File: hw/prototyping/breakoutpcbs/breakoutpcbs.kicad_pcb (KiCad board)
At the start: 2 copper layers, 34.5 x 20.8 mm, 48 parts, among them IC1 LTC2943IDD#TRPBF, J1 Conn_01x05, J2 Conn_01x05, J3 Conn_01x05, J4 Conn_01x05, Q1 BC847, Q2 BC337, Q3 BC337, Q4 SiS415DNT, Q5 BC847, Q6 BC337, Q7 BC847, U1 INA219BxDCN, U2 BD48ExxG, U3 BD48ExxG, U4 L7805, U5 XC6220B331MR, U6 MAX40200AUK

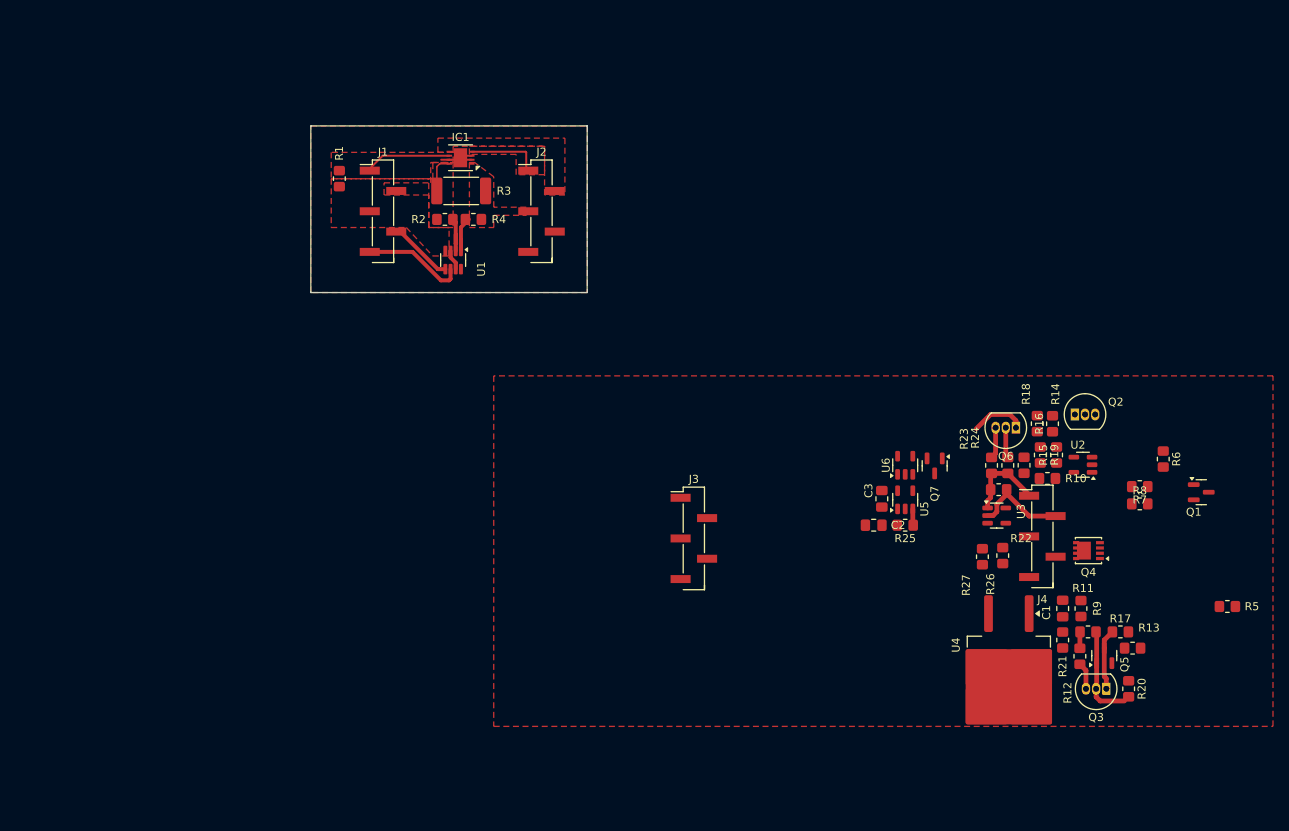
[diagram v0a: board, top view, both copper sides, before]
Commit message: created two other modules to test the switching between charging and runnig mode
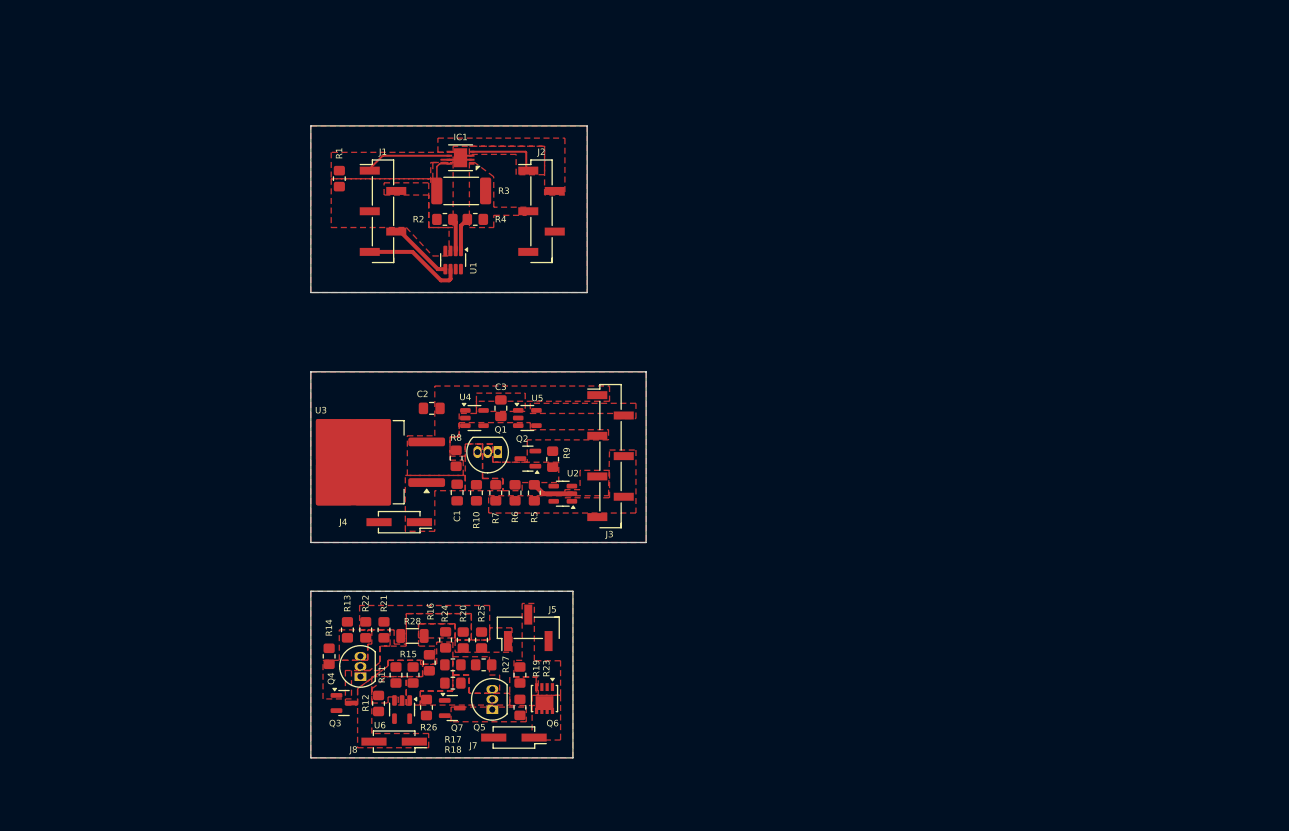
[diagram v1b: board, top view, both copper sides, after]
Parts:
- added J5: Conn_01x03, Connector_PinHeader_2.54mm:PinHeader_1x03_P2.54mm_Vertical_SMD_Pin1Left, F.Cu at (141.7, 118.1)
- added J7: Conn_01x02, Connector_PinHeader_2.54mm:PinHeader_2x01_P2.54mm_Vertical_SMD, F.Cu at (139.9, 131.8)
- added J8: Conn_01x02, Connector_PinHeader_2.54mm:PinHeader_2x01_P2.54mm_Vertical_SMD, F.Cu at (125.0, 132.3)
- added R28: 0R, Resistor_SMD:R_1206_3216Metric, F.Cu at (127.3, 119.1)
- J3: value Conn_01x05 -> Conn_01x07; footprint Connector_PinHeader_2.54mm:PinHeader_1x05_P2.54mm_Vertical_SMD_Pin1Left -> Connector_PinHeader_2.54mm:PinHeader_1x07_P2.54mm_Vertical_SMD_Pin1Left
- J4: value Conn_01x05 -> Conn_01x02; footprint Connector_PinHeader_2.54mm:PinHeader_1x05_P2.54mm_Vertical_SMD_Pin1Left -> Connector_PinHeader_2.54mm:PinHeader_2x01_P2.54mm_Vertical_SMD
- Q1, Q5: value BC847 -> BC337; footprint Package_TO_SOT_SMD:SOT-23 -> Package_TO_SOT_THT:TO-92_Inline
- Q2, Q3: value BC337 -> BC847; footprint Package_TO_SOT_THT:TO-92_Inline -> Package_TO_SOT_SMD:SOT-23
- Q4: value SiS415DNT -> BC337; footprint Package_SO:Vishay_PowerPAK_1212-8_Single -> Package_TO_SOT_THT:TO-92_Inline
- Q6: value BC337 -> SiS415DNT; footprint Package_TO_SOT_THT:TO-92_Inline -> Package_SO:Vishay_PowerPAK_1212-8_Single
- R11: value 4k2 -> 50k
- R12: value 4k2 -> 100k
- R13, R25: value 10k -> 0R
- R15, R23, R8: value 4k2 -> 10k
- R16, R24: value 4k2 -> 0R
- R17, R9: value 10k -> 4k2
- R18, R21, R7: value 0R -> 4k2
- R19: value 0R -> 10k
- R22: value 47k -> 4k2
- R5: value 50k -> 47k
- R6: value 100k -> 4k2
- U3: value BD48ExxG -> L7805; footprint Package_TO_SOT_SMD:SOT-23-5 -> Package_TO_SOT_SMD:TO-263-2
- U4: value L7805 -> XC6220B331MR; footprint Package_TO_SOT_SMD:TO-263-2 -> Package_TO_SOT_SMD:SOT-23-5
- U5: value XC6220B331MR -> MAX40200AUK
- U6: value MAX40200AUK -> BD48ExxG
- moved R13 98.2 mm to (119.1, 118.4), turned to -90 degrees
- moved Q3 95.3 mm to (118.7, 127.5), turned to 0 degrees
- moved Q4 92.4 mm to (120.8, 124.2), turned to 90 degrees
- moved R14 90.1 mm to (116.8, 121.7), turned to -90 degrees
- moved Q1 88.1 mm to (137.9, 96.1), turned to 180 degrees
- moved R12 87.9 mm to (123.0, 127.6), turned to 90 degrees
- moved R5 87.8 mm to (142.5, 101.2), turned to 90 degrees
- moved R11 86.7 mm to (125.2, 124.0), turned to 90 degrees
- moved R8 85.6 mm to (132.7, 96.9), turned to -90 degrees
- moved R15 85.0 mm to (127.3, 124.0)
- moved R21 84.8 mm to (123.7, 118.4)
- moved R17 83.7 mm to (132.3, 125.0)
- moved R16 83.4 mm to (129.4, 122.5), turned to -90 degrees
- moved R20 83.4 mm to (133.6, 119.6), turned to 90 degrees
- moved R6 81.1 mm to (140.1, 101.2), turned to 90 degrees
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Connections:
- C1 pad 1: /power_switch_bb/ONOFF -> /power_switch_bbB/ONOFF
- C1 pad 2: GND -> GND2
- C2 pad 2: GND -> GND2
- C3 pad 1: Net-(U5-VOUT) -> Net-(U4-VOUT)
- C3 pad 2: GND -> GND2
- J3 pad 2: /power_switch_bb/ONOFF -> +3V3_1
- J3 pad 3: /power_switch_bb/VBATT -> /power_switch_bbB/RUNNING
- J3 pad 4: +3V3 -> /power_switch_bbB/EN
- J3 pad 5: GND -> /power_switch_bbB/VBUS
- J4 pad 1: /power_switch_bb/EN -> /power_switch_bbB/ONOFF
- J4 pad 2: /power_switch_bb/VBUS -> GND2
- Q1 pad 1: Net-(Q1-B) -> /power_switch_bbB/RUNNING
- Q1 pad 2: GND -> Net-(Q1-B)
- Q1 pad 3: Net-(Q1-C) -> Net-(Q1-E)
- Q2 pad 1: Net-(Q1-C) -> Net-(Q1-B)
- Q2 pad 2: Net-(Q1-B) -> GND2
- Q2 pad 3: Net-(Q2-E) -> /power_switch_bbB/RUNNING
- Q3 pad 1: Net-(Q3-C) -> Net-(Q3-B)
- Q3 pad 2: Net-(Q3-B) -> GND1
- Q3 pad 3: Net-(Q3-E) -> Net-(Q3-C)
- Q4 pad 1: /power_switch_bb/VBATT -> Net-(Q3-C)
- Q4 pad 2: /power_switch_bb/VBATT -> Net-(Q3-B)
- Q4 pad 3: /power_switch_bb/VBATT -> Net-(Q4-E)
- Q5 pad 1: Net-(Q3-B) -> Net-(Q5-C)
- Q5 pad 2: GND -> Net-(Q5-B)
- Q5 pad 3: Net-(Q3-C) -> Net-(Q5-E)
- Q6 pad 1: /power_switch_bb/RUNNING -> /power_switch_bbA/VBATT
- Q6 pad 2: Net-(Q6-B) -> /power_switch_bbA/VBATT
- Q6 pad 3: Net-(Q6-E) -> /power_switch_bbA/VBATT
- Q7 pad 1: Net-(Q6-B) -> Net-(Q5-B)
- Q7 pad 2: GND -> GND1
- Q7 pad 3: /power_switch_bb/RUNNING -> Net-(Q5-C)
- R10 pad 1: Net-(Q1-C) -> GND2
- R10 pad 2: Net-(U2-VOUT) -> Net-(Q1-E)
- R11 pad 1: Net-(U2-VOUT) -> Net-(U6-VDD)
- R11 pad 2: Net-(Q3-B) -> /power_switch_bbA/ONOFF
- R12 pad 1: Net-(U2-VOUT) -> GND1
- R12 pad 2: Net-(Q3-E) -> Net-(U6-VDD)
- R13 pad 1: /power_switch_bb/VBATT -> GND1
- R13 pad 2: Net-(Q4-G) -> Net-(Q4-E)
- R14 pad 1: /power_switch_bb/EN -> GND1
- R14 pad 2: Net-(Q1-C) -> Net-(Q3-B)
- R15 pad 1: Net-(R15-Pad1) -> Net-(U6-VOUT)
- R15 pad 2: Net-(Q1-B) -> /power_switch_bbA/ONOFF
- R16 pad 1: Net-(R15-Pad1) -> Net-(Q3-C)
- R16 pad 2: Net-(Q2-E) -> Net-(U6-VOUT)
- R17 pad 1: Net-(Q3-C) -> Net-(U6-VOUT)
- R17 pad 2: Net-(Q4-G) -> Net-(Q5-B)
- R18 pad 1: Net-(R15-Pad1) -> Net-(U6-VOUT)
- R18 pad 2: Net-(U2-VOUT) -> Net-(Q5-E)
- R19 pad 1: /power_switch_bb/EN -> /power_switch_bbA/VBATT
- R19 pad 2: Net-(R15-Pad1) -> Net-(Q6-G)
- R20 pad 1: GND -> /power_switch_bbA/EN1
- R20 pad 2: Net-(Q3-B) -> Net-(Q3-C)
- R21 pad 1: GND -> Net-(R21-Pad1)
- R21 pad 2: Net-(Q3-E) -> Net-(Q3-B)
- R22 pad 1: /power_switch_bb/EN -> Net-(R21-Pad1)
- R22 pad 2: /power_switch_bb/VBUS -> Net-(Q4-E)
- R23 pad 1: /power_switch_bb/EN -> Net-(Q5-C)
- R23 pad 2: Net-(Q6-B) -> Net-(Q6-G)
- R24 pad 1: /power_switch_bb/EN -> Net-(R24-Pad1)
- R24 pad 2: Net-(Q6-E) -> Net-(U6-VOUT)
- R25 pad 1: /power_switch_bb/RUNNING -> /power_switch_bbA/EN1
- R25 pad 2: +5V -> Net-(R21-Pad1)
- R26 pad 1: GND -> GND1
- R26 pad 2: Net-(Q6-B) -> Net-(Q5-B)
- R27 pad 1: GND -> GND1
- R27 pad 2: Net-(Q6-E) -> Net-(Q5-E)
- R5 pad 1: Net-(U2-VDD) -> /power_switch_bbB/EN
- R5 pad 2: /power_switch_bb/ONOFF -> /power_switch_bbB/VBUS
- R6 pad 1: GND -> /power_switch_bbB/EN
- R6 pad 2: Net-(U2-VDD) -> Net-(Q1-B)
- R7 pad 1: GND -> /power_switch_bbB/EN
- R7 pad 2: Net-(Q2-E) -> Net-(Q1-E)
- R8 pad 1: GND -> /power_switch_bbB/RUNNING
- R8 pad 2: Net-(Q1-B) -> +5V
- R9 pad 1: Net-(U2-VOUT) -> GND2
- R9 pad 2: /power_switch_bb/ONOFF -> Net-(Q1-B)
- U2 pad 1: Net-(U2-VOUT) -> /power_switch_bbB/EN
- U2 pad 2: Net-(U2-VDD) -> /power_switch_bbB/VBUS
- U2 pad 3: GND -> GND2
- U3 pad 1: /power_switch_bb/EN -> /power_switch_bbB/ONOFF
- U3 pad 2: /power_switch_bb/VBUS -> GND2
- U3 pad 3: GND -> +5V
- U4 pad 1: /power_switch_bb/ONOFF -> +5V
- U4 pad 2: GND -> GND2
- U4 pad 3: +5V -> /power_switch_bbB/RUNNING
- U5 pad 1: +5V -> Net-(U4-VOUT)
- U5 pad 2: GND -> GND2
- U5 pad 3: /power_switch_bb/RUNNING -> /power_switch_bbB/RUNNING
- U5 pad 5: Net-(U5-VOUT) -> +3V3_1
- U6 pad 1: Net-(U5-VOUT) -> Net-(U6-VOUT)
- U6 pad 2: GND -> Net-(U6-VDD)
- U6 pad 3: /power_switch_bb/RUNNING -> GND1
- U6 pad 4: unconnected-(U6-NC-Pad4) -> (no net)
- U6 pad 5: +3V3 -> (no net)
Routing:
- net /power_switch_bb/VBUS: track 12.4 -> 0.00 mm
- net Net-(Q3-B): track 11.8 -> 0.00 mm
- net /power_switch_bb/EN: track 10.6 -> 0.00 mm
- net /power_switch_bb/RUNNING: track 8.95 -> 0.00 mm
- net Net-(Q3-C): track 7.64 -> 0.00 mm
- net /power_switch_bbB/VBUS: track 0.00 -> 5.15 mm
- net Net-(Q6-E): track 3.93 -> 0.00 mm
- net Net-(Q6-B): track 3.82 -> 0.00 mm
- net Net-(Q3-E): track 3.38 -> 0.00 mm
- net GND: track 8.07 -> 5.53 mm
- net Net-(U2-VOUT): track 2.05 -> 0.00 mm
- net Net-(U1-IN-): track 5.26 -> 4.09 mm
- net Net-(U1-IN+): track 4.88 -> 4.27 mm
- added copper zone on F.Cu, net +3V3_1
- added copper zone on F.Cu, net +5V
- added copper zone on F.Cu, net +7.5V
- added copper zone on F.Cu, net /power_manager_bb/BALARM
- added copper zone on F.Cu, net /power_switch_bbA/EN1
- added copper zone on F.Cu, net /power_switch_bbA/ONOFF
- added copper zone on F.Cu, net /power_switch_bbA/VBATT
- added copper zone on F.Cu, net /power_switch_bbB/EN
- added copper zone on F.Cu, net /power_switch_bbB/ONOFF
- added copper zone on F.Cu, net /power_switch_bbB/RUNNING
- added copper zone on F.Cu, net /power_switch_bbB/VBUS
- added copper zone on F.Cu, net GND1
- added copper zone on F.Cu, net GND2
- added copper zone on F.Cu, net Net-(Q1-B)
- added copper zone on F.Cu, net Net-(Q1-E)
- added copper zone on F.Cu, net Net-(Q3-B)
- added copper zone on F.Cu, net Net-(Q3-C)
- added copper zone on F.Cu, net Net-(Q4-E)
- added copper zone on F.Cu, net Net-(Q5-B)
- added copper zone on F.Cu, net Net-(Q5-C)
- added copper zone on F.Cu, net Net-(Q5-E)
- added copper zone on F.Cu, net Net-(Q6-G)
- added copper zone on F.Cu, net Net-(R21-Pad1)
- added copper zone on F.Cu, net Net-(R24-Pad1)
- added copper zone on F.Cu, net Net-(U4-VOUT)
- added copper zone on F.Cu, net Net-(U6-VDD)
- added copper zone on F.Cu, net Net-(U6-VOUT)
- removed copper zone on F.Cu, net (none)
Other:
- board size 34.5 x 20.8 mm -> 41.9 x 79 mm

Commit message: refactoring of the current boards and two added to test the whole circuit
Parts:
- added C4: 22uF, Capacitor_SMD:C_0805_2012Metric_Pad1.18x1.45mm_HandSolder, F.Cu at (104.7, 83.5)
- added C5: 22uF, Capacitor_SMD:C_0805_2012Metric_Pad1.18x1.45mm_HandSolder, F.Cu at (107.0, 83.5)
- added C6: 22uF, Capacitor_SMD:C_0805_2012Metric_Pad1.18x1.45mm_HandSolder, F.Cu at (109.2, 83.5)
- added J10: Conn_01x03_MountingPin, Connector_JST:JST_XH_S3B-XH-SM4-TB_1x03-1MP_P2.50mm_Horizontal, F.Cu at (210.6, 135.1)
- added J11: Conn_01x07, Connector_PinSocket_2.54mm:PinSocket_1x07_P2.54mm_Vertical_SMD_Pin1Left, F.Cu at (216.7, 75.9)
- added J12: Conn_01x07, Connector_PinSocket_2.54mm:PinSocket_1x07_P2.54mm_Vertical_SMD_Pin1Left, F.Cu at (201.4, 75.9)
- added J13: Conn_01x06, Connector_PinHeader_2.54mm:PinHeader_1x06_P2.54mm_Vertical_SMD_Pin1Left, F.Cu at (194.6, 80.3)
- added J14: Conn_01x02, Connector_PinHeader_2.54mm:PinHeader_2x01_P2.54mm_Vertical_SMD, F.Cu at (210.3, 126.7)
- added J15: Conn_01x04, Connector_PinHeader_2.54mm:PinHeader_1x04_P2.54mm_Vertical_SMD_Pin1Left, F.Cu at (187.6, 80.3)
- added J16: Screw_Terminal_01x04, TerminalBlock_Phoenix:TerminalBlock_Phoenix_MPT-0,5-4-2.54_1x04_P2.54mm_Horizontal, F.Cu at (215.9, 46.2)
- added J17: Conn_01x05, Connector_PinHeader_2.54mm:PinHeader_1x05_P2.54mm_Vertical_SMD_Pin1Left, F.Cu at (216.2, 59.2)
- added J18: Screw_Terminal_01x04, TerminalBlock_Phoenix:TerminalBlock_Phoenix_MPT-0,5-4-2.54_1x04_P2.54mm_Horizontal, F.Cu at (204.0, 46.2)
- added J19: Conn_01x02, Connector_PinHeader_2.54mm:PinHeader_2x01_P2.54mm_Vertical_SMD, F.Cu at (190.5, 135.4)
- added J6: Conn_01x05, Connector_PinHeader_2.54mm:PinHeader_1x05_P2.54mm_Vertical_SMD_Pin1Left, F.Cu at (185.0, 134.4)
- added J9: Screw_Terminal_01x02, TerminalBlock_Phoenix:TerminalBlock_Phoenix_MKDS-1,5-2_1x02_P5.00mm_Horizontal, F.Cu at (195.4, 136.1)
- added M1: ~, chinese_modules:USBC_charger, F.Cu at (200.1, 111.0)
- added M2: ~, chinese_modules:RF_controller, F.Cu at (187.5, 57.4)
- added Q10: BC337, Package_TO_SOT_THT:TO-92_Inline, F.Cu at (202.9, 59.2)
- added Q11: BC847, Package_TO_SOT_SMD:SOT-23, F.Cu at (203.2, 51.9)
- added Q8: BC337, Package_TO_SOT_THT:TO-92_Inline, F.Cu at (200.2, 127.6)
- added Q9: BC847, Package_TO_SOT_SMD:SOT-23, F.Cu at (206.1, 122.9)
- added R29: 4k2, Resistor_SMD:R_0805_2012Metric_Pad1.20x1.40mm_HandSolder, F.Cu at (92.5, 133.6)
- added R30: 10k, Resistor_SMD:R_0805_2012Metric_Pad1.20x1.40mm_HandSolder, F.Cu at (105.4, 132.6)
- added R31: 10k, Resistor_SMD:R_0805_2012Metric_Pad1.20x1.40mm_HandSolder, F.Cu at (107.5, 97.0)
- added R32: 10k, Resistor_SMD:R_0805_2012Metric_Pad1.20x1.40mm_HandSolder, F.Cu at (109.8, 92.4)
- added R33: 0R, Resistor_SMD:R_1206_3216Metric, F.Cu at (90.4, 126.2)
- added R34: 4k2, Resistor_SMD:R_0805_2012Metric_Pad1.20x1.40mm_HandSolder, F.Cu at (195.8, 129.3)
- added R35: 4k2, Resistor_SMD:R_0805_2012Metric_Pad1.20x1.40mm_HandSolder, F.Cu at (193.8, 127.3)
- added R36: 0R, Resistor_SMD:R_1206_3216Metric, F.Cu at (199.1, 122.4)
- added R37: 4k2, Resistor_SMD:R_0805_2012Metric_Pad1.20x1.40mm_HandSolder, F.Cu at (209.6, 122.9)
- added R38: 0R, Resistor_SMD:R_0805_2012Metric_Pad1.20x1.40mm_HandSolder, F.Cu at (192.0, 129.3)
- added R39: 12k, Resistor_SMD:R_0805_2012Metric_Pad1.20x1.40mm_HandSolder, F.Cu at (210.6, 54.4)
- added R40: 4k7, Resistor_SMD:R_0805_2012Metric_Pad1.20x1.40mm_HandSolder, F.Cu at (208.8, 87.9)
- added R41: 10k, Resistor_SMD:R_0805_2012Metric_Pad1.20x1.40mm_HandSolder, F.Cu at (209.8, 84.8)
- added R42: 4k2, Resistor_SMD:R_0805_2012Metric_Pad1.20x1.40mm_HandSolder, F.Cu at (203.2, 63.5)
- added R43: 4k2, Resistor_SMD:R_0805_2012Metric_Pad1.20x1.40mm_HandSolder, F.Cu at (205.5, 63.5)
- added R44: 4k2, Resistor_SMD:R_0805_2012Metric_Pad1.20x1.40mm_HandSolder, F.Cu at (203.2, 55.1)
- added R45: 0R, Resistor_SMD:R_0805_2012Metric_Pad1.20x1.40mm_HandSolder, F.Cu at (206.0, 54.4)
- added R46: 0R, Resistor_SMD:R_0805_2012Metric_Pad1.20x1.40mm_HandSolder, F.Cu at (95.3, 88.8)
- added R47: 4k2, Resistor_SMD:R_0805_2012Metric_Pad1.20x1.40mm_HandSolder, F.Cu at (103.4, 92.6)
- added R48: 0R, Resistor_SMD:R_0805_2012Metric_Pad1.20x1.40mm_HandSolder, F.Cu at (97.6, 87.1)
- added R49: 10k, Resistor_SMD:R_0805_2012Metric_Pad1.20x1.40mm_HandSolder, F.Cu at (189.8, 123.3)
- added R50: 0R, Resistor_SMD:R_1206_3216Metric, F.Cu at (197.4, 126.0)
- added R51: 4k2, Resistor_SMD:R_0805_2012Metric_Pad1.20x1.40mm_HandSolder, F.Cu at (202.9, 122.9)
- added R52: 10k, Resistor_SMD:R_0805_2012Metric_Pad1.20x1.40mm_HandSolder, F.Cu at (190.8, 126.2)
- added R53: 4k7, Resistor_SMD:R_0805_2012Metric_Pad1.20x1.40mm_HandSolder, F.Cu at (208.3, 54.4)
- added R54: 0R, Resistor_SMD:R_0805_2012Metric_Pad1.20x1.40mm_HandSolder, F.Cu at (200.2, 54.6)
- added R55: 4k2, Resistor_SMD:R_0805_2012Metric_Pad1.20x1.40mm_HandSolder, F.Cu at (200.9, 63.5)
- added R56: 0R, Resistor_SMD:R_0805_2012Metric_Pad1.20x1.40mm_HandSolder, F.Cu at (200.2, 58.4)
- added R57: 10k, Resistor_SMD:R_0805_2012Metric_Pad1.20x1.40mm_HandSolder, F.Cu at (109.8, 94.7)
- added R58: 200R, Resistor_SMD:R_0805_2012Metric_Pad1.20x1.40mm_HandSolder, F.Cu at (189.7, 121.4)
- added R59: 200R, Resistor_SMD:R_0805_2012Metric_Pad1.20x1.40mm_HandSolder, F.Cu at (188.7, 126.2)
- added R60: 0R, Resistor_SMD:R_1206_3216Metric, F.Cu at (182.9, 121.7)
- added U7: BD48ExxG, Package_TO_SOT_SMD:SOT-23-5, F.Cu at (110.3, 89.6)
- added U8: MAX40200AUK, Package_TO_SOT_SMD:SOT-23-5, F.Cu at (185.9, 125.5)
- added U9: MAX40200AUK, Package_TO_SOT_SMD:SOT-23-5, F.Cu at (193.9, 122.4)
- R20: value 4k2 -> 0R
- R5: value 47k -> 10k
- moved R9 49.6 mm to (95.3, 94.4), turned to 90 degrees
- moved U2 42.5 mm to (105.2, 89.6)
- moved U4 41.7 mm to (94.1, 83.4)
- moved C3 41.4 mm to (97.6, 83.2)
- moved Q2 41.2 mm to (101.4, 88.2), turned to 90 degrees
- moved U5 41.1 mm to (101.4, 83.5)
- moved R10 40.9 mm to (94.5, 97.5), turned to 0 degrees
- moved C1 40.4 mm to (93.0, 94.4)
- moved R8 40.2 mm to (93.1, 90.1)
- moved J4 40.2 mm to (86.0, 98.2)
- moved Q1 39.6 mm to (98.6, 91.6), turned to -90 degrees
- moved R7 39.3 mm to (98.6, 97.0), turned to 180 degrees
- moved C2 39.1 mm to (92.0, 80.5)
- moved U3 38.9 mm to (84.1, 86.1), turned to 90 degrees
- moved U1 38.5 mm to (95.5, 61.0)
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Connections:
- J3 pad 5: /power_switch_bbB/VBUS -> /power_switch_bbB/EN
- J3 pad 6: /power_switch_bbB/EN -> GND2
- J3 pad 7: GND2 -> /power_switch_bbB/VBUS
- Q1 pad 1: /power_switch_bbB/RUNNING -> Net-(Q1-C)
- Q2 pad 3: /power_switch_bbB/RUNNING -> Net-(Q1-C)
- R5 pad 1: /power_switch_bbB/EN -> Net-(U2-VOUT)
- R6 pad 1: /power_switch_bbB/EN -> Net-(U2-VOUT)
- R7 pad 1: /power_switch_bbB/EN -> Net-(U2-VOUT)
- U2 pad 1: /power_switch_bbB/EN -> Net-(U2-VOUT)
- U2 pad 2: /power_switch_bbB/VBUS -> Net-(U2-VDD)
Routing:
- net +3V3_2: track 0.00 -> 11.9 mm
- net /battery_charger/CHARGING (BLUE): track 0.00 -> 11.7 mm
- net /battery_charger/EN2: track 0.00 -> 5.26 mm
- net /power_switch_bbB/VBUS: track 5.15 -> 0.00 mm
- net Net-(Q5-C): track 0.00 -> 3.94 mm
- net Net-(U9-VDD): track 0.00 -> 2.06 mm
- net Net-(U9-EN): track 0.00 -> 2.05 mm
- added copper zone on F.Cu, net +3V3_3
- added copper zone on F.Cu, net +5V_1
- added copper zone on F.Cu, net +7V5_1
- added copper zone on F.Cu, net /battery_charger/CHARGED (GREEN)
- added copper zone on F.Cu, net /battery_charger/VBUS1
- added copper zone on F.Cu, net /break_control/BALARM1
- added copper zone on F.Cu, net /break_control/BUTTON
- added copper zone on F.Cu, net /break_control/BUZZ
- added copper zone on F.Cu, net /break_control/BUZZER
- added copper zone on F.Cu, net /break_control/CHARGING1
- added copper zone on F.Cu, net /break_control/DCKI
- added copper zone on F.Cu, net /break_control/DI
- added copper zone on F.Cu, net /break_control/RF SWITCH
- added copper zone on F.Cu, net /break_control/SCL
- added copper zone on F.Cu, net /break_control/SDA
- added copper zone on F.Cu, net /break_control/SERVO
- added copper zone on F.Cu, net /break_control/VBUS2
- added copper zone on F.Cu, net /break_control/VEXT
- added copper zone on F.Cu, net GND3
- added copper zone on F.Cu, net GND4
- added copper zone on F.Cu, net Net-(J10-Pin_2)
- added copper zone on F.Cu, net Net-(J10-Pin_3)
- added copper zone on F.Cu, net Net-(J12-Pin_6)
- added copper zone on F.Cu, net Net-(J14-Pin_2)
- added copper zone on F.Cu, net Net-(M1-LED)
- added copper zone on F.Cu, net Net-(M1-Vin)
- added copper zone on F.Cu, net Net-(M2-D0)
- added copper zone on F.Cu, net Net-(Q1-C)
- added copper zone on F.Cu, net Net-(Q10-B)
- added copper zone on F.Cu, net Net-(Q10-C)
- added copper zone on F.Cu, net Net-(Q10-E)
- added copper zone on F.Cu, net Net-(Q8-B)
- added copper zone on F.Cu, net Net-(Q8-C)
- added copper zone on F.Cu, net Net-(Q8-E)
- added copper zone on F.Cu, net Net-(R36-Pad1)
- added copper zone on F.Cu, net Net-(U2-VDD)
- added copper zone on F.Cu, net Net-(U2-VOUT)
- added copper zone on F.Cu, net Net-(U8-OUT)
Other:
- board size 41.9 x 79 mm -> 143.8 x 99.6 mm

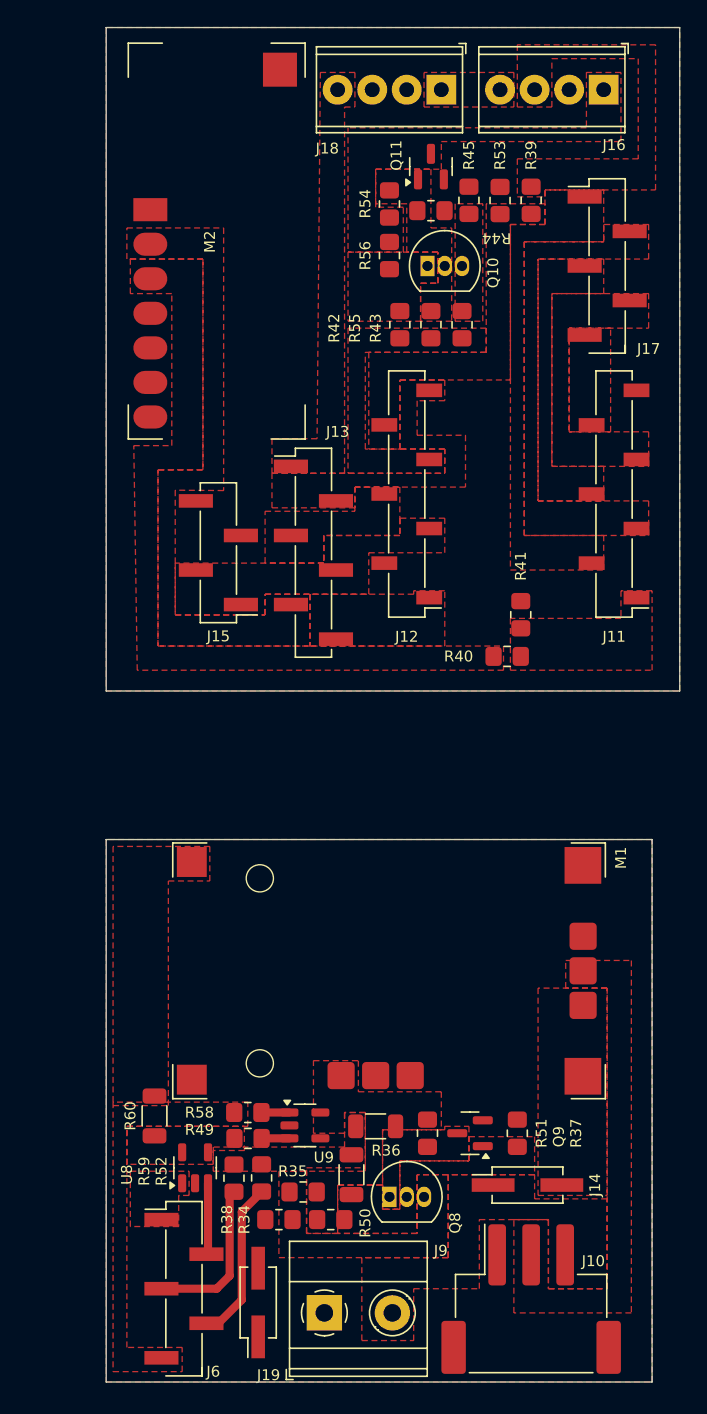
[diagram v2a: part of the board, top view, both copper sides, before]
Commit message: fixed wrong pinout on rf module and updated footprints
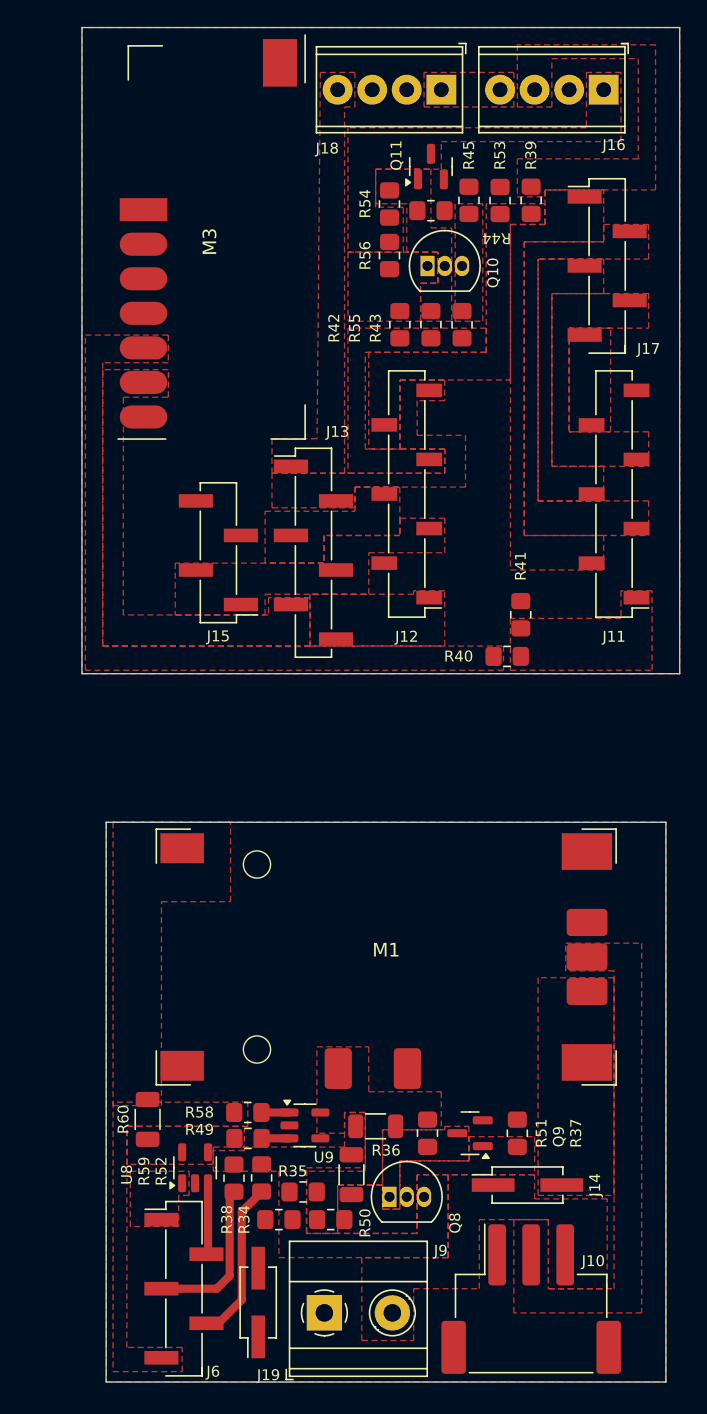
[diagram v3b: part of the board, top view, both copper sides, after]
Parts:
- removed M2: ~, chinese_modules:RF_controller
- added M3: ~, chinese_modules:RF_controller, F.Cu at (187.5, 57.4)
- moved M1 1.04 mm to (199.9, 110.0)
- moved R60 0.57 mm to (182.4, 121.9)
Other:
- outline, holes or cut-outs redrawn
